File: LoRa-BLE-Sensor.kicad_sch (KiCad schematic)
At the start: 124 parts, among them J1 SHF-105-01-X-D-SM, J2 Battery_Cell, J3 Conn_01x06_Socket, J4 Screw_Terminal_01x03, J5 Screw_Terminal_01x08, J6 Screw_Terminal_01x08, J7 Conn_01x10_Pin, K1 SRD-05VDC-SL-C, Q1 DMN67D7L, Q10 SQ2389ES, Q11 DMN62D0UDW-7, Q12 DMN62D0UDW-7, Q2 DMN67D7L, Q3 DMN67D7L, Q4 DMN67D7L, Q5 DMN67D7L, Q6 DMN67D7L, Q7 DMN67D7L, Q8 DMN67D7L, Q9 SQ2389ES, SW1 SW_Push, SW2 SW_Push, SW3 SW_Push, U1 RAK4630, U2 NPM1300-QEAA-R, U3 TLV61046ADBVR, U4 TLV61046ADBVR

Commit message: Schematic + JPEG
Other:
- note added: "RAK4630"
- company: (none) -> Cyber Jungle
- title: (none) -> LoRa-BLE-Sensor
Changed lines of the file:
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@@
 	(generator_version "8.0")
 	(paper "A3")
+	(title_block
+		(title "LoRa-BLE-Sensor")
+		(date "2025-03-05")
+		(rev "1")
+		(company "Cyber Jungle")
+	)
 	(junction
 		(at 53.34 161.29)
@@
 		)
 	)
-	(text "NPM1300"
+	(text "RAK4630"
 		(exclude_from_sim no)
 		(at 20.32 24.13 0)

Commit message: updated schematic
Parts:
- R30, R31, R32, R33, R34: value 500K -> 300K
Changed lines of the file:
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@@
 			)
 		)
-		(property "Value" "500K"
+		(property "Value" "300K"
 			(at 223.52 171.704 90)
 			(effects
@@
 			)
 		)
-		(property "Value" "500K"
+		(property "Value" "300K"
 			(at 231.14 175.2599 0)
 			(effects
@@
 			)
 		)
-		(property "Value" "500K"
+		(property "Value" "300K"
 			(at 185.42 96.5199 0)
 			(effects
@@
 			)
 		)
-		(property "Value" "500K"
+		(property "Value" "300K"
 			(at 231.14 213.3599 0)
 			(effects
@@
 			)
 		)
-		(property "Value" "500K"
+		(property "Value" "300K"
 			(at 223.52 209.804 90)
 			(effects

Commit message: BOM
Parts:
- D18: value GREEN -> RED

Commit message: beginning V1.1 deisgn
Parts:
- removed D18: RED, LED_SMD:LED_0402_1005Metric, symbol Device:LED
- removed D19: M7, User_Actives:DIOM5327X240N, symbol User_Actives:M7
- removed D3, D4, D7, D8: UDD32C24L01, User_Actives:SOD2612X120N, symbol User_Actives:UDD32C24L01
- removed J4: Screw_Terminal_01x03, User_Connectors:PhoenixContact_MCV_1x03_P5.08mm_Vertical, symbol Connector:Screw_Terminal_01x03
- removed J5, J6: Screw_Terminal_01x08, Connector_Phoenix_MC:PhoenixContact_MCV_1,5_8-G-3.81_1x08_P3.81mm_Vertical, symbol Connector:Screw_Terminal_01x08
- removed K1: SRD-05VDC-SL-C, User_Actives:RELAY_SRD-05VDC-SL-C, symbol User_Actives:SRD-05VDC-SL-C
- removed R11, R12, R15, R16, R41, R7, R8: 10K, Resistor_SMD:R_0402_1005Metric, symbol Device:R_US
- added C26, C27: 300p, Capacitor_SMD:C_0402_1005Metric, symbol Device:C
- added J5, J6: Screw_Terminal_01x06, Connector_Phoenix_MC:PhoenixContact_MCV_1,5_6-G-3.81_1x06_P3.81mm_Vertical, symbol Connector:Screw_Terminal_01x06
- R3, R4: value 10K -> 0R; footprint Resistor_SMD:R_0402_1005Metric -> Inductor_SMD:L_0402_1005Metric
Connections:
- net BUT1: no longer U1.13 (P0.09)
- net GND: now also C26.2, C27.2, J5.6 (Pin_6), J6.6 (Pin_6); no longer J7.10 (Pin_10), J7.5 (Pin_5)
- net NPM_IO1: no longer U1.12 (P0.10)
- net NPM_IO2: no longer U1.11 (P0.21)
- net VDD: no longer J7.2 (Pin_2), J7.7 (Pin_7), Q3.1 (G), Q4.1 (G), Q7.1 (G), Q8.1 (G), R3.1, R4.1
- net V_SENSOR1: now also Q3.1 (G), Q4.1 (G); no longer D14.1 (K), D16.1, J7.1 (Pin_1), Q9.2 (S), R18.1
- net V_SENSOR2: now also Q7.1 (G), Q8.1 (G); no longer D15.1 (K), D17.1, J7.6 (Pin_6), Q10.2 (S), R28.1
- net D0_IN renamed SENSOR1_D1
- net SENSOR1_D1: now also Q4.2 (S), J5.4 (Pin_4); no longer Q1.3 (D)
- net D0_NRF renamed SENSOR1_D1_NRF
- net D1_IN renamed SENSOR1_D2
- net SENSOR1_D2: now also Q3.2 (S), J5.5 (Pin_5); no longer Q2.3 (D)
- net D1_NRF renamed SENSOR1_D2_NRF
- net D2_IN: no longer names the net of Q3.3 (D)
- net D2_IN: now also Q2.3 (D)
- removed net D2_NRF: J7.3 (Pin_3), Q3.2 (S), R3.2, U1.24 (P0.25)
- net D3_IN: no longer names the net of Q4.3 (D)
- net D3_IN: now also Q1.3 (D)
- removed net D3_NRF: J7.4 (Pin_4), Q4.2 (S), R4.2, U1.23 (P0.24)
- net D4_IN renamed SENSOR2_D1
- net SENSOR2_D1: now also Q7.2 (S), J6.4 (Pin_4); no longer Q5.3 (D)
- net D4_NRF renamed SENSOR2_D1_NRF
- net D5_IN renamed SENSOR2_D2
- net SENSOR2_D2: now also Q8.2 (S), J6.5 (Pin_5); no longer Q6.3 (D)
- net D5_NRF renamed SENSOR2_D2_NRF
- net D6_IN: no longer names the net of Q7.3 (D)
- net D6_IN: now also Q5.3 (D)
- removed net D6_NRF: J7.8 (Pin_8), Q7.2 (S), U1.28 (P1.04)
- net D7_IN: no longer names the net of Q8.3 (D)
- net D7_IN: now also Q6.3 (D)
- removed net D7_NRF: J7.9 (Pin_9), Q8.2 (S), U1.27 (P1.03)
- net I0_IN renamed SENSOR1_IIN
- net SENSOR1_IIN: now also J5.2 (Pin_2)
- net I1_IN renamed SENSOR2_IIN
- net SENSOR2_IIN: now also J6.2 (Pin_2)
- net V0_IN renamed SENSOR1_VIN
- net SENSOR1_VIN: now also J5.3 (Pin_3)
- net V1_IN renamed SENSOR2_VIN
- net SENSOR2_VIN: now also J6.3 (Pin_3)
- net V_RELAY renamed V_BUCK1
- new net: C27.1, R3.2
- new net: C26.1, R4.2
- new net NFC1: R3.1, U1.13 (P0.09)
- new net NFC2: R4.1, U1.12 (P0.10)
- new net VOUT_SENSOR1: D14.1 (K), D16.1, J5.1 (Pin_1), Q9.2 (S), R18.1
- new net VOUT_SENSOR2: D15.1 (K), D17.1, J6.1 (Pin_1), Q10.2 (S), R28.1
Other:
- note added: "NFC1 -> P0.09 NFC2 -> P0.10"
- note removed: "Relay"
- moved on the sheet: C4, D1, D2, D5, D6, J1, J7, Q1, Q2, Q5, Q6, R1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

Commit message: update
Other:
- moved on the sheet: C5, C6, C7, C8, D10, D11, D12, D14, D15, D16, D17, D9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

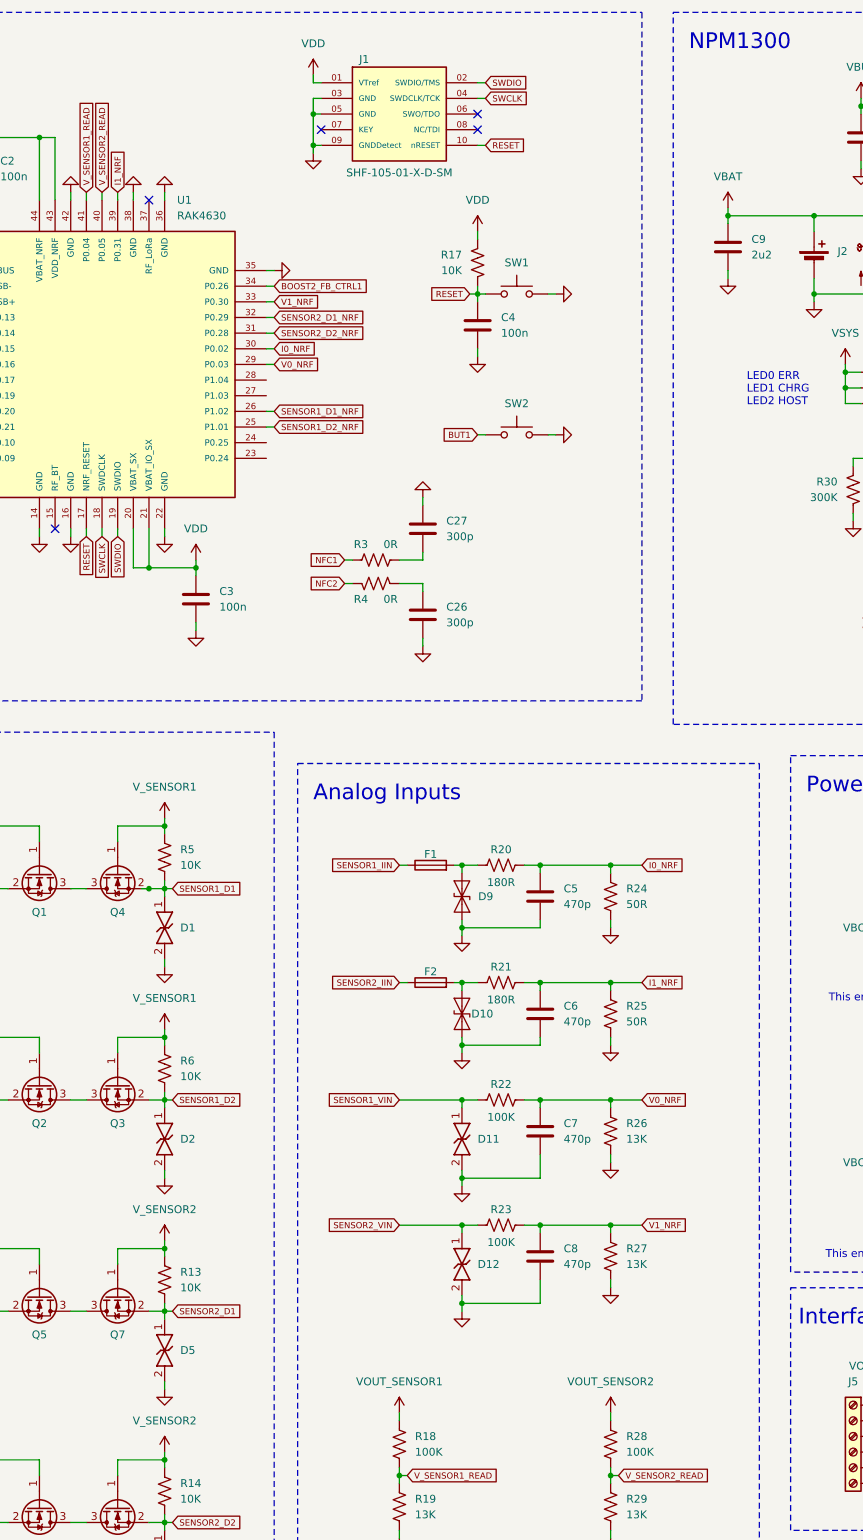
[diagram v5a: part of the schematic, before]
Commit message: renaming pin labels
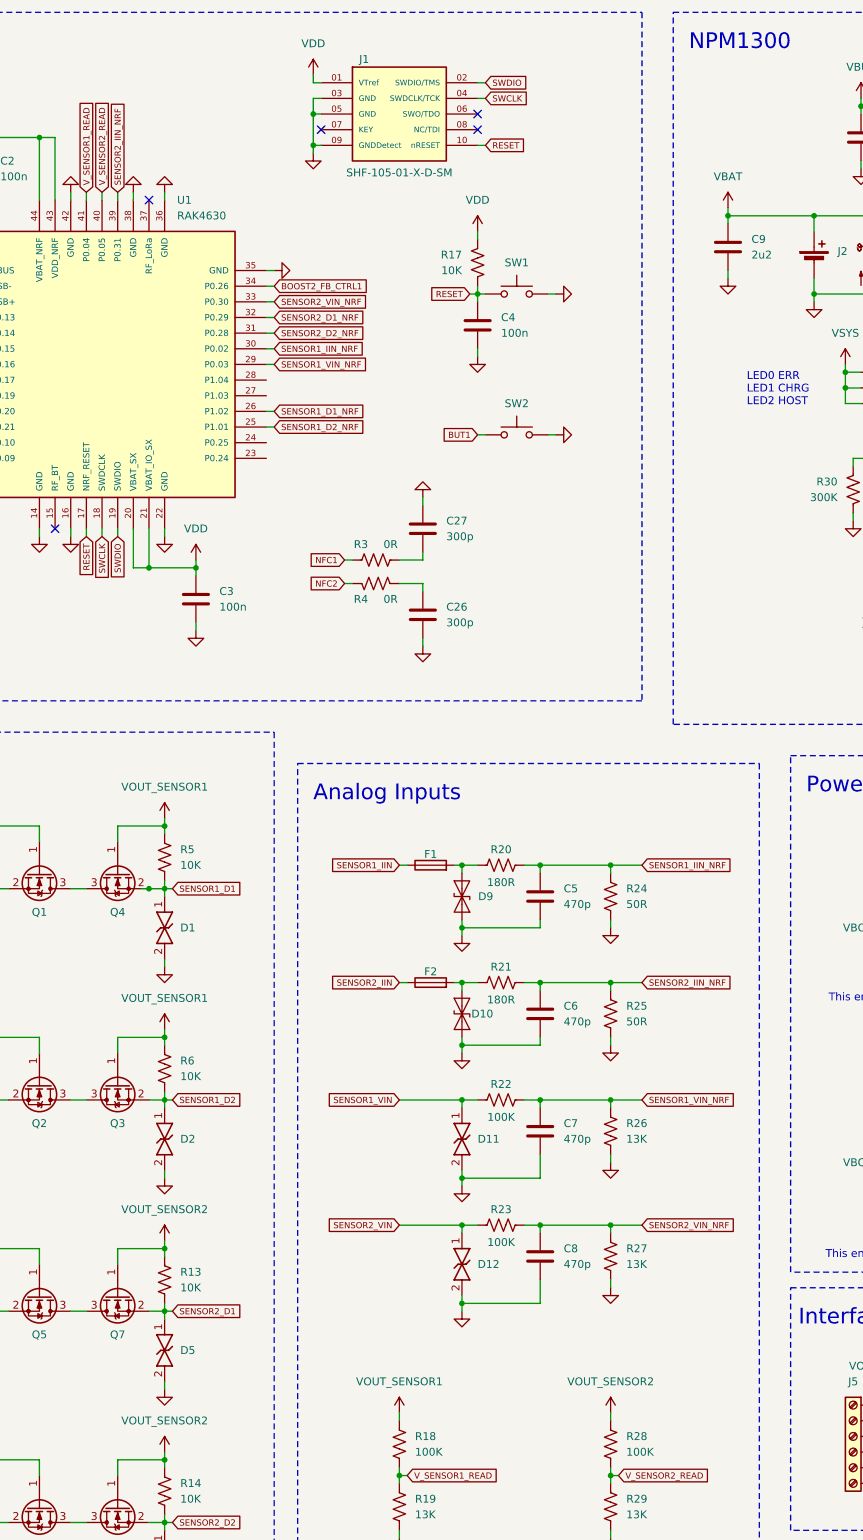
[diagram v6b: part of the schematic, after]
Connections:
- net V_SENSOR1 is gone; now on net VOUT_SENSOR1: Q3.1 (G), Q4.1 (G), R5.1, R6.1
- net V_SENSOR2 is gone; now on net VOUT_SENSOR2: Q7.1 (G), Q8.1 (G), R13.1, R14.1
- net I0_NRF renamed SENSOR1_IIN_NRF
- net I1_NRF renamed SENSOR2_IIN_NRF
- net V0_NRF renamed SENSOR1_VIN_NRF
- net V1_NRF renamed SENSOR2_VIN_NRF

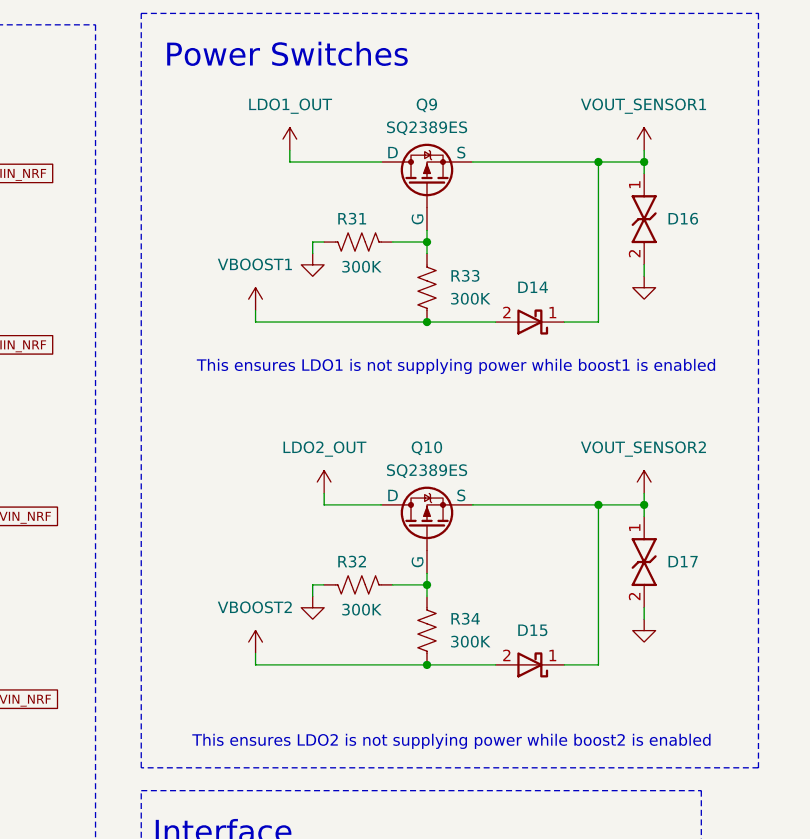
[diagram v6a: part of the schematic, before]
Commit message: removed power switch voltage dividers
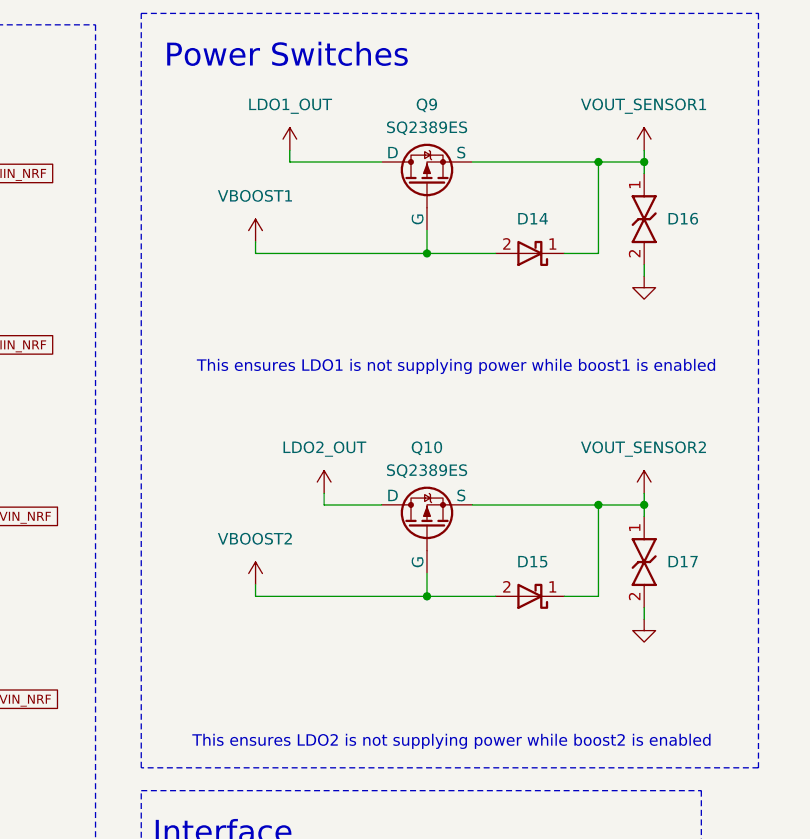
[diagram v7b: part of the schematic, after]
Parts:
- removed R31, R32, R33, R34: 300K, Resistor_SMD:R_0402_1005Metric, symbol Device:R_US
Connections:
- net VBOOST1: now also Q9.1 (G)
- net VBOOST2: now also Q10.1 (G)
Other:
- moved on the sheet: D14, D15

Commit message: added sensor 3
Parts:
- added C28: 10u, Capacitor_SMD:C_0603_1608Metric, symbol Device:C
- added C29: 10u, Capacitor_SMD:C_0805_2012Metric, symbol Device:C
- added D3: BAT54W-HG3-08, User_Actives:SOD3716X135N, symbol User_Actives:BAT54W-HG3-08
- added D7: PRTR5V0U2X,215, User_Actives:PRTR5V0U2X, symbol User_Actives:PRTR5V0U2X,215
- added J4: Screw_Terminal_01x04, Connector_Phoenix_MC:PhoenixContact_MCV_1,5_4-G-3.81_1x04_P3.81mm_Vertical, symbol Connector:Screw_Terminal_01x04
- added L5: 10U, Inductor_SMD:L_1008_2520Metric, symbol Device:L
- added Q13: SQ2389ES, Package_TO_SOT_SMD:SOT-23-3, symbol User_Actives:SQ2319CES
- added R11: 71K5, Resistor_SMD:R_0402_1005Metric, symbol Device:R_US
- added R7: 10K, Resistor_SMD:R_0402_1005Metric, symbol Device:R_US
- added R8: 383K, Resistor_SMD:R_0402_1005Metric, symbol Device:R_US
- added U5: TLV61046ADBVR, User_Power:SOT95P280X145-6N, symbol User_Power:TLV61046ADBVR
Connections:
- net GND: now also C28.2, C29.2, D7.1 (GND), J4.4 (Pin_4), R11.2, R7.2, U5.2 (GND)
- net VSYS: now also C28.1, L5.1, U5.6 (VIN)
- net V_BUCK1: now also Q13.3 (D)
- new net: L5.2, U5.1 (SW)
- new net BOOST3_EN: R7.1, U5.4 (EN)
- new net BOOST3_FB: R11.1, R8.2, U5.3 (FB)
- new net SENSOR3_D1_NRF: D7.2 (I/O1), J4.2 (Pin_2)
- new net SENSOR3_D2_NRF: D7.3 (I/O2), J4.3 (Pin_3)
- new net VBOOST3: C29.1, D3.2 (A), Q13.1 (G), R8.1, U5.5 (VOUT)
- new net VOUT_SENSOR3: D3.1 (K), D7.4 (VCC), J4.1 (Pin_1), Q13.2 (S)
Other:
- note added: "Boost 3"
- note added: "SENSOR 3 ESD"
- note added: "Sensor 3 is only used for digital interfaces that work at 3.3V logic and can be powered with 3.3V or 5V"
- note added: "This ensures BUCK1 is not supplying power while boost2 is enabled"
- moved on the sheet: C18, C19, C24, C25, C5, C6, C7, C8, D1, D10, D11, D12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
